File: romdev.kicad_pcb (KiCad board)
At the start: 2 copper layers, 90.6 x 77.8 mm, 55 parts, among them J1 AVR-ISP, J2 USB_B_Micro, J3 idc2k, J4 dip2k, J5 idc32k, J6 dip32k, J7 SYSRST, U1 ATmega328P, U10 conn2k, U11 conn32k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

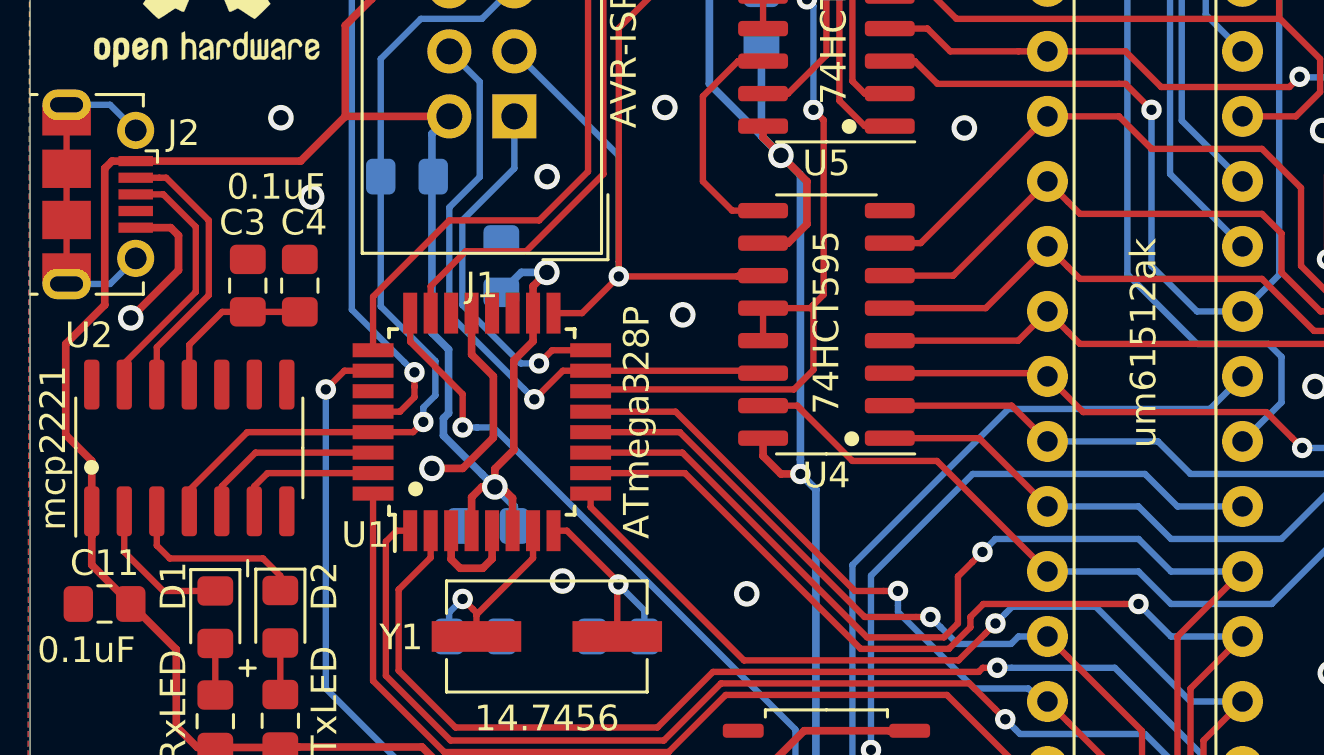
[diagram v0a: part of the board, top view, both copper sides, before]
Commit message: fixed swapped RX/TX lines
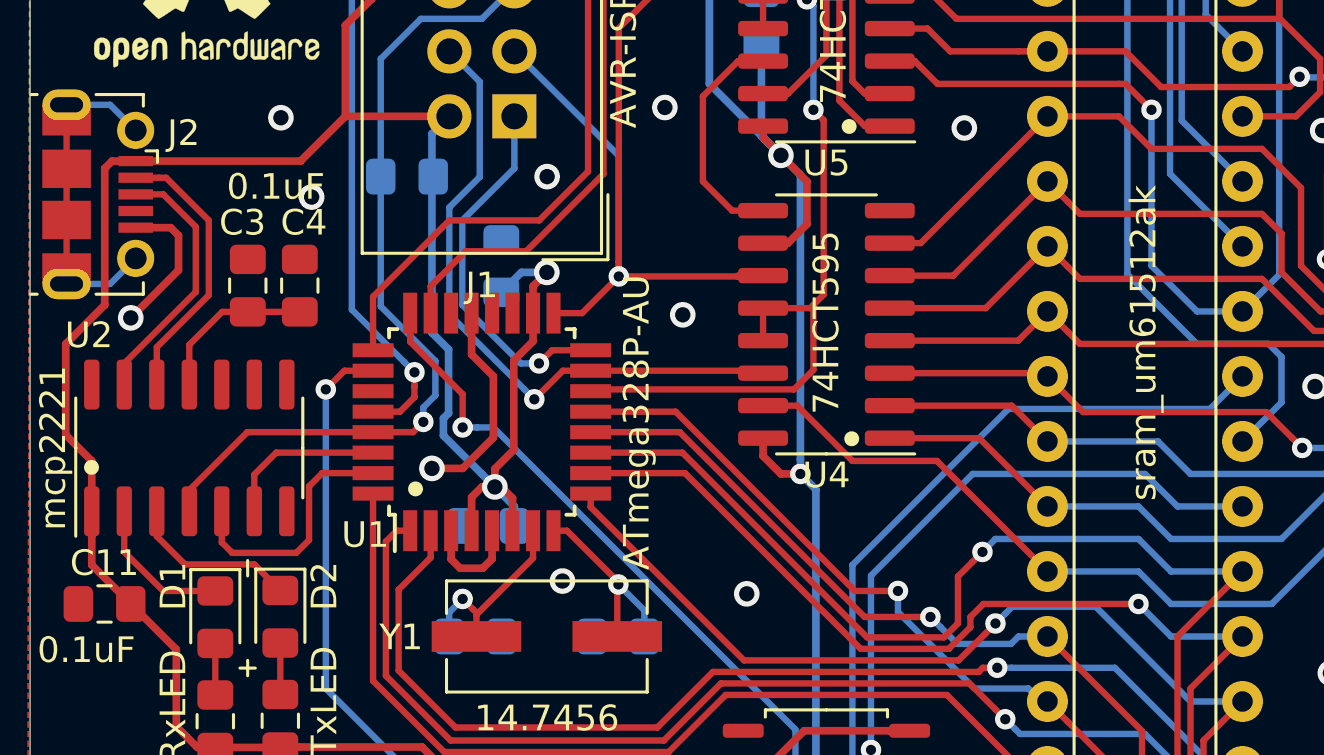
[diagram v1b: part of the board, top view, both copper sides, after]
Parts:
- U1: value ATmega328P -> ATmega328P-AU
- U6: value um61512ak -> sram_um61512ak
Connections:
- U2 pad 5: /RX -> /TX
- U2 pad 6: /TX -> /RX
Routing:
- net /TX: track 5.83 -> 9.82 mm
- net /RX: track 7.43 -> 6.43 mm
- net Net-(D2-Pad1): track 7.23 -> 6.68 mm

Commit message: - fixed mistake tying half the tri-state buffer bits to always on - fixed firmware bugs, now it can program and readback memory correctly
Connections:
- U7 pad 19: GND -> /PGM
- U8 pad 19: GND -> /PGM
- U9 pad 19: GND -> /PGM
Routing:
- net /PGM: track 130.8 -> 150.5 mm, vias 5 -> 7
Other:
- board text added: "PCB rev2 - 11/10/2020"
- board text removed: "PCB rev1 - 19/5/2020"

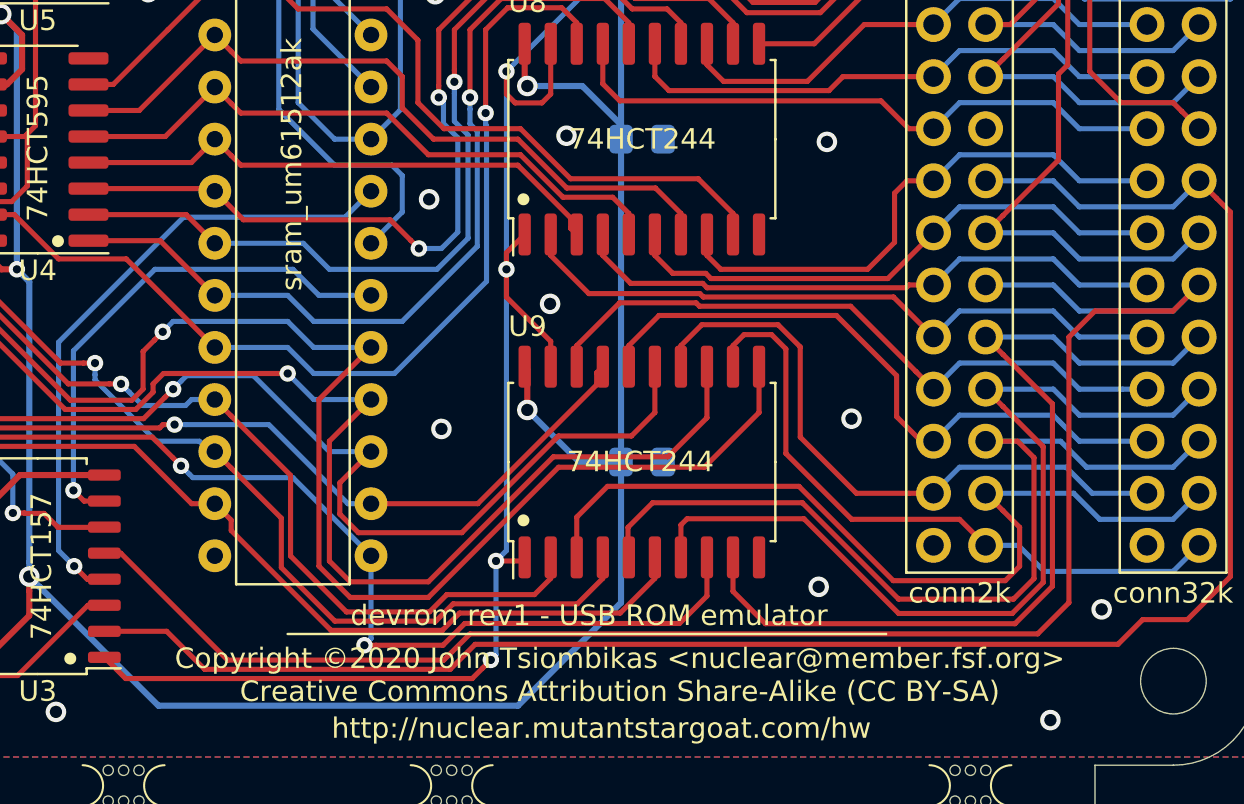
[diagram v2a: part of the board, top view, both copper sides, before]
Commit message: fixed data bus output buffer enable
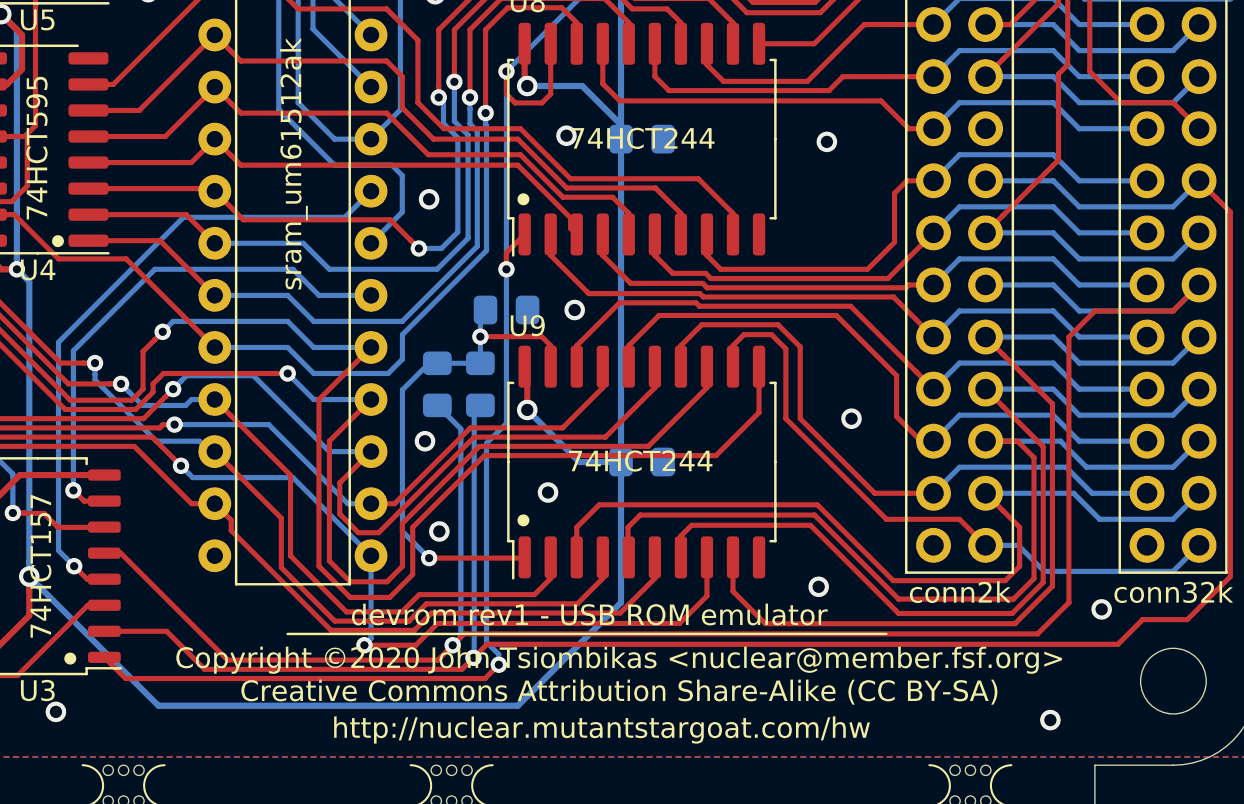
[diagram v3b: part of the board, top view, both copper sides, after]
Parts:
- added D3: 1N4148, Diode_SMD:D_0805_2012Metric_Pad1.15x1.40mm_HandSolder, B.Cu at (206.5, 57.4)
- added D4: 1N4148, Diode_SMD:D_0805_2012Metric_Pad1.15x1.40mm_HandSolder, B.Cu at (204.4, 57.4)
- added R8: 4K7, Resistor_SMD:R_0805_2012Metric_Pad1.15x1.40mm_HandSolder, B.Cu at (207.8, 53.8)
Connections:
- U9 pad 1: /PGM -> Net-(D3-Pad1)
- U9 pad 19: /PGM -> Net-(D3-Pad1)
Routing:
- net Net-(D3-Pad1): track 0.00 -> 25.1 mm, vias 0 -> 2
- net /~SYSOE: track 89.0 -> 101.4 mm, vias 0 -> 1
- net /~SYSCS: track 82.2 -> 94.5 mm, vias 0 -> 1
- net /PGM: track 150.5 -> 144.2 mm, vias 7 -> 6
- net /D7: track 71.4 -> 72.8 mm
- net /SYSD4: track 42.1 -> 41.1 mm
- net /SYSD3: track 32.3 -> 31.3 mm
- net /D5: track 55.0 -> 54.3 mm
- net /SYSD6: track 44.0 -> 43.4 mm
- net /SYSD2: track 31.2 -> 30.7 mm
- net GND: vias 30 -> 32
